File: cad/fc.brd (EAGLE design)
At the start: 52.4 x 77.6 mm, 23 parts

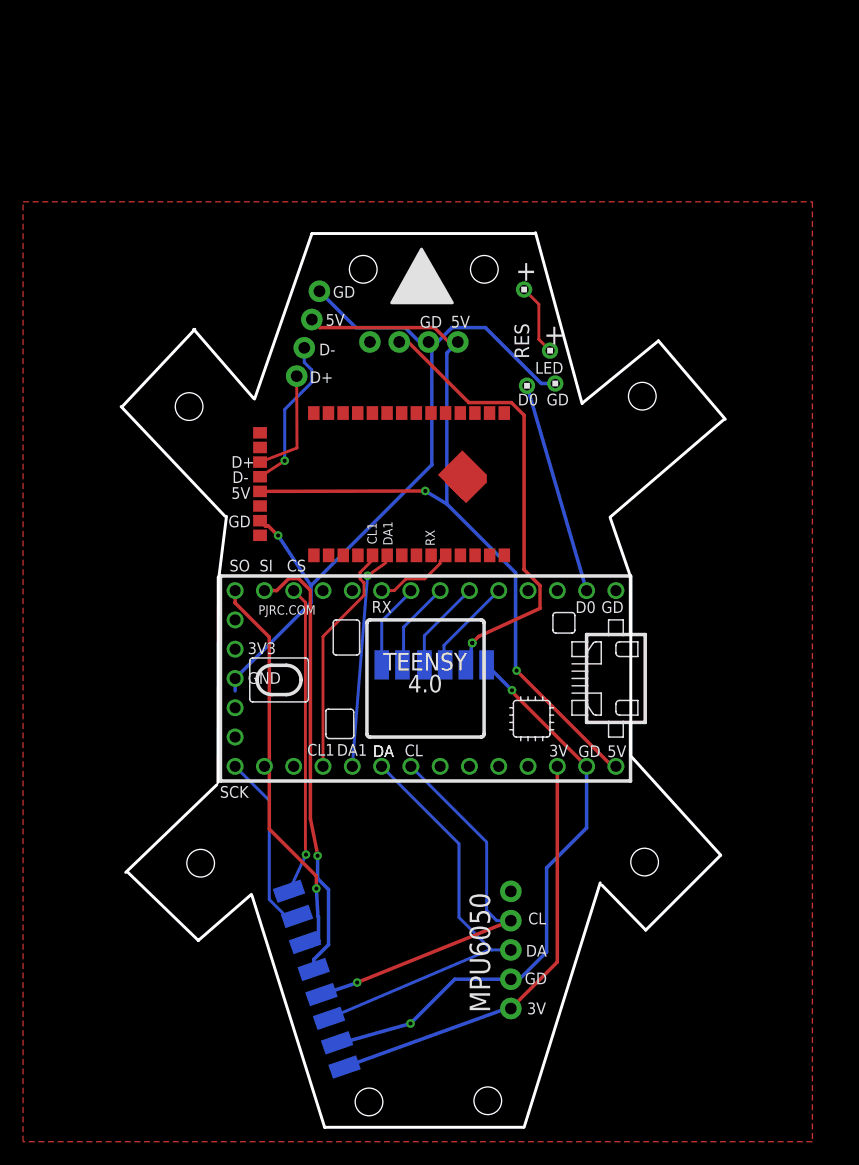
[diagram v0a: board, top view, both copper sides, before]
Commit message: new file:   cad/fc.brd
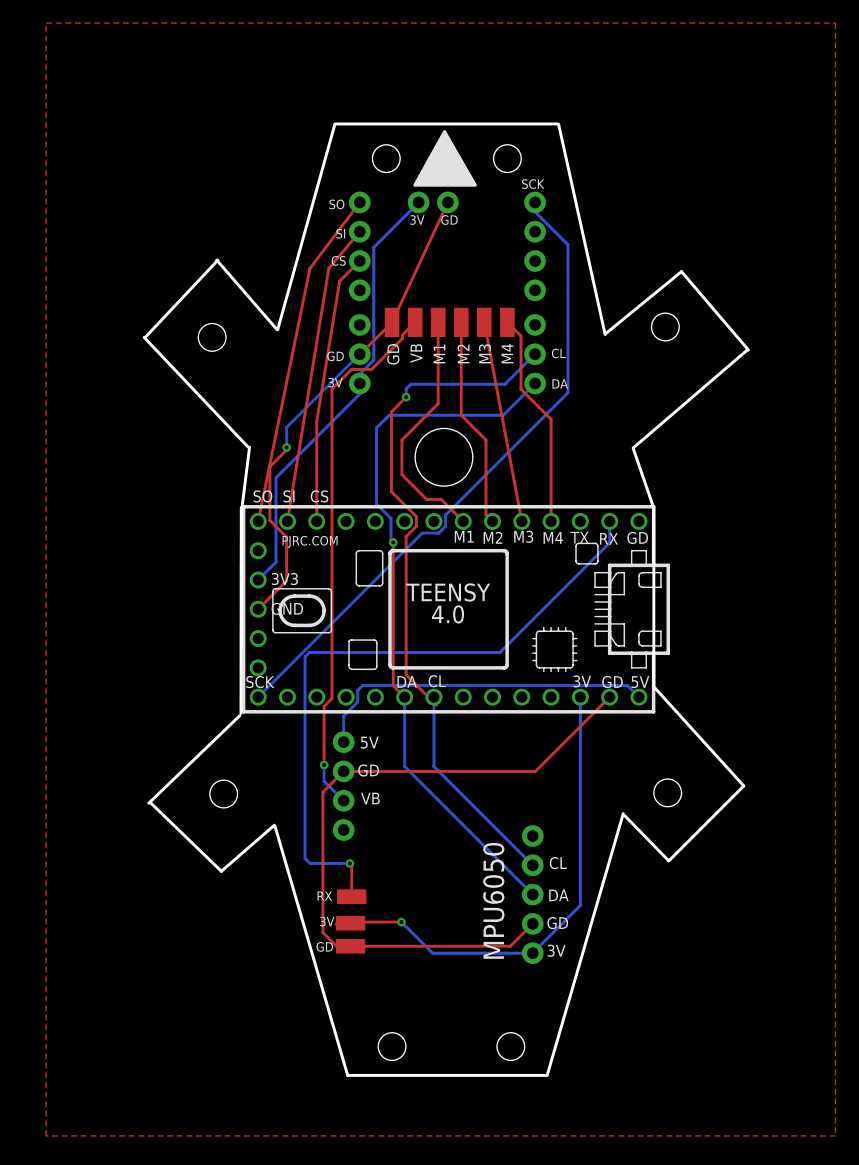
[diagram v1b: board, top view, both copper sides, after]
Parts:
- removed 3V2, 3V3, CS, GD1, GD2, RX1, RX2, SCK: (no value), wirepad:SMD1,27-2,54
- removed J2: (no value), SparkFun-Connectors:1X04_NO_SILK
- removed U$2: TINYPICO-NANO-CONNECTOR, TinyPICO_NANO_Eagle:TINYPICO-NANO-CONNECTOR
- removed U$3, U$4, U$6, U$7: 1X1, headers(2mm):1X1
- added 3V, GD, RX: (no value), wirepad:SMD1,27-2,54
- added PMW1, PMW2: (no value), SparkFun-Connectors:1X04_NO_SILK
- added PMW3: (no value), SparkFun-Connectors:1X02_NO_SILK
- added VL1, VL2: (no value), SparkFun-Connectors:1X03_NO_SILK
- moved REG 36.1 mm to (27.6, 34.4), turned to 270 degrees
- moved M1 31.6 mm to (41.8, 70.8), flipped to the top
- moved GND 30.8 mm to (31.8, 70.8), flipped to the top
- moved M2 30.5 mm to (39.8, 70.8), flipped to the top
- moved VBAT 30.0 mm to (33.8, 70.8), flipped to the top
- moved M3 29.9 mm to (37.8, 70.8), flipped to the top
- moved M4 29.7 mm to (35.8, 70.8), flipped to the top
- moved U$1 6.32 mm to (36.7, 45.9)
- moved J1 5.16 mm to (44.0, 16.1)
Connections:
- removed net D+: J2.4, U$2.D+
- removed net D-: J2.3, U$2.D-
- removed net G2: U$1.GND
- removed net LED_R_IN: U$1.0/RX, U$3.1
- removed net LED_R_OUT: U$4.1, U$6.1
- removed net SCL1: U$1.16/A2, U$2.IO22
- removed net SDA1: U$1.17/A3, U$2.IO21
- removed net VB: REG.3, U$2.VBAT, VBAT.1
- new net TX: U$1.1/TX
- new net VBAT: REG.3, VBAT.1
- net 3V3: now also 3V.1, PMW3.1, U$1.3V3_LN, VL2.1; no longer 3V2.1, U$2.3V3
- net 5V: no longer J2.2, U$2.5V
- net CS: now also PMW2.3; no longer CS.1
- net GND: now also GD.1, PMW3.2, U$1.GND, VL2.2; no longer GD1.1, J2.1, U$2.GND$1, U$2.GND$2, U$2.GND$3, U$2.GND$4, U$7.1
- net M1: now also M4.1, U$1.5; no longer M1.1, U$1.6
- net M2: now also M3.1, U$1.4/CANRX; no longer M2.1, U$1.5
- net M3: now also M2.1, U$1.3/CANTX; no longer M3.1, U$1.4/CANRX
- net M4: now also M1.1, U$1.2; no longer M4.1, U$1.3/CANTX
- net MISO: now also PMW2.1; no longer 3V3.1
- net MOSI: now also PMW2.2; no longer RX2.1
- net RX: now also RX.1, U$1.0/RX; no longer U$1.7, U$2.TX
- net SCK: now also PMW1.1; no longer SCK.1
- net SCL: now also VL1.2; no longer GD2.1
- net SDA: now also VL1.1; no longer RX1.1
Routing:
- net RX: track 6.96 -> 56.9 mm, vias 0 -> 1
- net VBAT: track 0.00 -> 46.5 mm, vias 0 -> 1
- net 3V3: track 38.0 -> 81.6 mm, vias 0 -> 1
- net 5V: track 73.3 -> 30.0 mm, vias 2 -> 0
- net SCK: track 15.8 -> 56.0 mm
- net VB: track 38.9 -> 0.00 mm, vias 2 -> 0
- net SCL: track 35.3 -> 60.9 mm
- net SDA: track 36.8 -> 61.4 mm, vias 0 -> 1
- net SCL1: track 20.4 -> 0.00 mm
- net SDA1: track 18.5 -> 0.00 mm, vias 1 -> 0
- net LED_R_IN: track 18.5 -> 0.00 mm
- net GND: track 120.3 -> 102.7 mm, vias 3 -> 1
- net M1: track 7.49 -> 21.5 mm
- net D-: track 13.6 -> 0.00 mm, vias 1 -> 0
- net MOSI: track 38.7 -> 26.4 mm, vias 1 -> 0
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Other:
- board size 52.4 x 77.6 mm -> 52.4 x 82.5 mm
- board text added: "PMW3901"
- board text added: "TX"
- board text added: "VL53LL1"
- board text removed: "+"
- board text removed: "CL1"
- board text removed: "D+"
- board text removed: "D-"
- board text removed: "D0"
- board text removed: "DA1"
- board text removed: "LED"
- board text removed: "RES"
